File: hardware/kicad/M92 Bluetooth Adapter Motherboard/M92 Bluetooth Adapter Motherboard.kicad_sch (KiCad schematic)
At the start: 27 parts, among them IC1 PIC18F27Q43-I/SO, J2 Conn_Handset_RJ45, J6 Conn_MCU_Programming, J7 Conn_BT_Module, J8 Conn_MCU_IO_UART, Q2 PN2222ATA / MMBT2222A

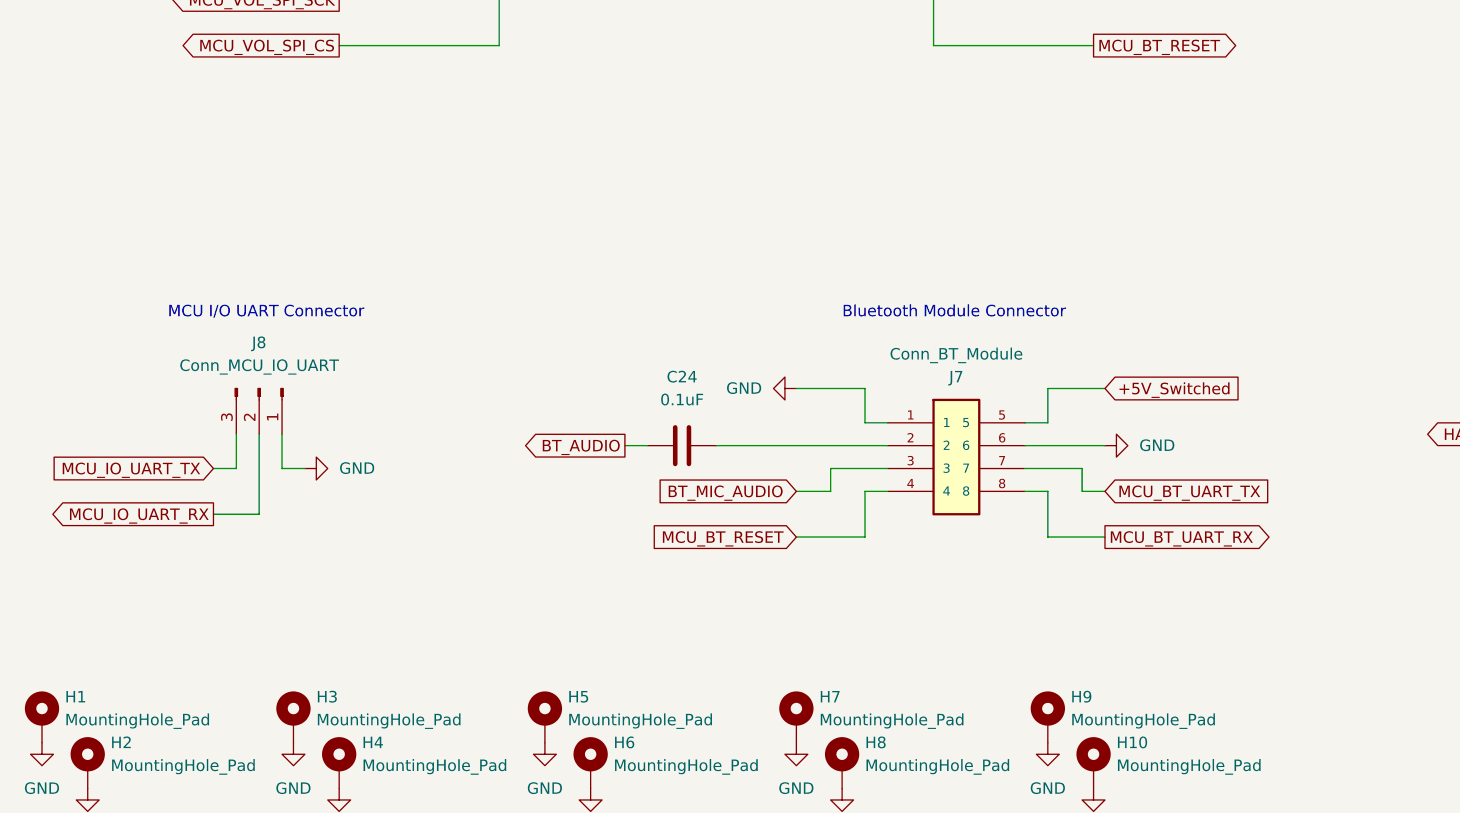
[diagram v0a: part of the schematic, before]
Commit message: Partial motherboard PCB updates for test fitting
This is a partial update to the motherboard PCB layout just so I can get some prototype boards manufactured and test fit with some updated/relocated components before committing to laying out the new custom battery/power management circuitry.

* Removed representation of Dayton Audio battery module PCB (will be replaced by custom battery circuitry in future).
* Relocated battery holders, and updated their footprints for sturdier part.
* Added pin headers for mounting the new programming port PCB.
* Adjusted positions of several mounting holes in attempt to match reality better (based on actual fitment of the PCB).
* Adjusted position of BT module connector slightly right in attempt to match reality better (based on actual fitment of the PCB).
* Adjusted footprint of mic jack to use oval PTH.
* Adjusted mic jack position further toward front edge of board to protrude more like original car phone mic jack.
* Added custom 3D models for BT module connector, RJ45 socket, and coax antenna port.
* Added coax antenna port and programming port to the PCB layout for spatial reference (not on schematic)
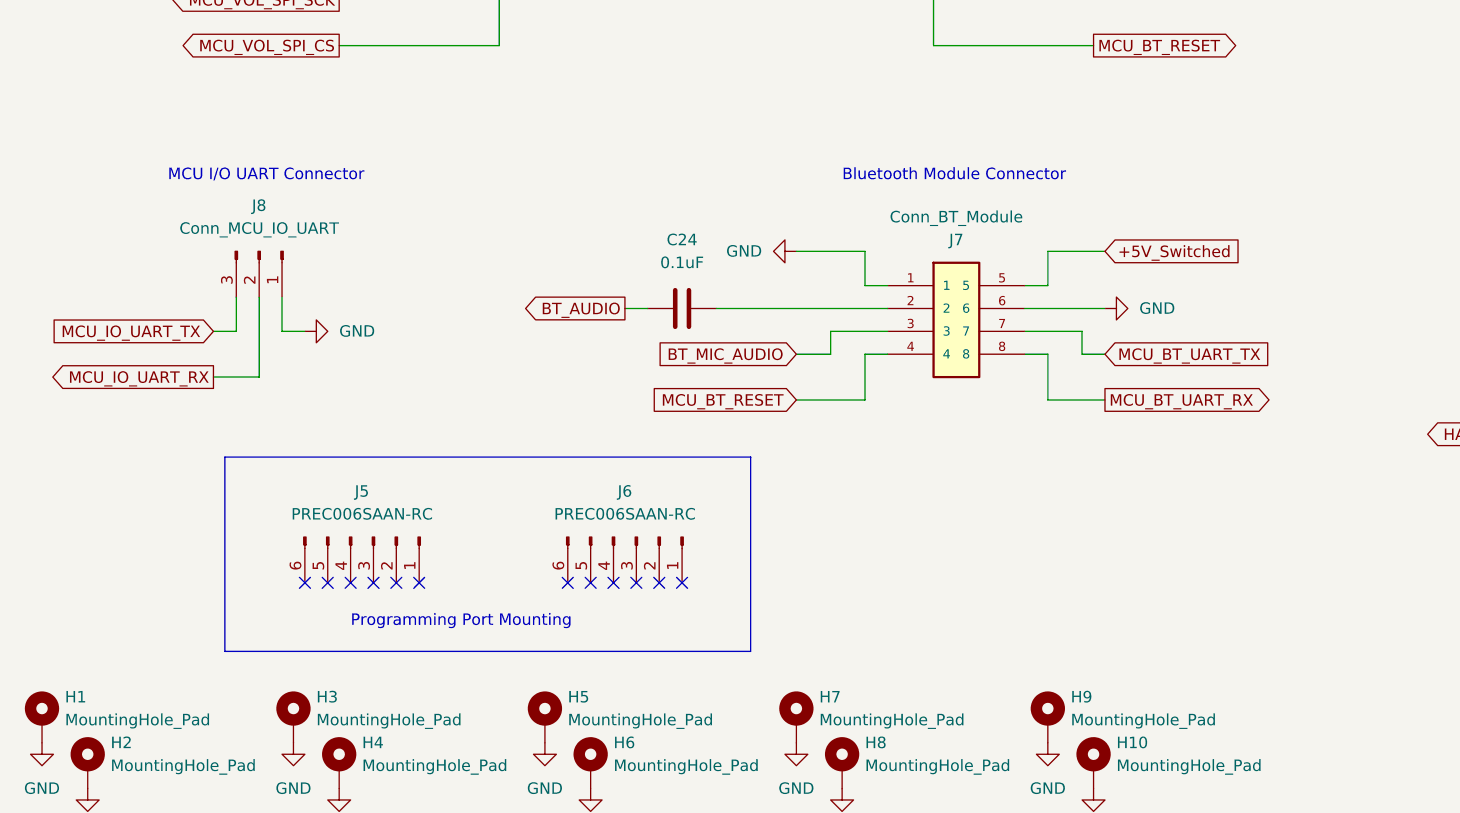
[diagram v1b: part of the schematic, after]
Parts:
- added J5, J6: PREC006SAAN-RC, Connector_PinHeader_2.54mm:PinHeader_1x06_P2.54mm_Vertical, symbol Connector:Conn_01x06_Pin
- H1, H10, H3, H4, H6, H7, H8, H9: footprint MountingHole:MountingHole_3.2mm_M3_Pad_Via -> MountingHole:MountingHole_3.2mm_M3_ISO14580_Pad
- J2: footprint GLXN88MBLK -> M92 Bluetooth Adapter Motherboard:KYCON_GLX-N-88M; symbol SamacSys_Parts:GLX-N-88M-BLK -> M92 Bluetooth Adapter Motherboard:GLX-N-88M; Manufacturer_Part_Number GLX-N-88M -> GLX-N-88M-BLK; Mouser Part Number 806-GLX-N-88M -> 806-GLX-N-88M-BLK; Mouser Price/Stock https://www.mouser.com/ProductDetail/Kycon/GLX-N-88M?qs=1jN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 -> https://www.mouser.com/ProductDetail/Kycon/GLX-N-88M-BLK?qs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
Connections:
- no-connect marks 2 -> 14
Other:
- note added: "Programming Port Mounting"
- moved on the sheet: C24, J7, J8

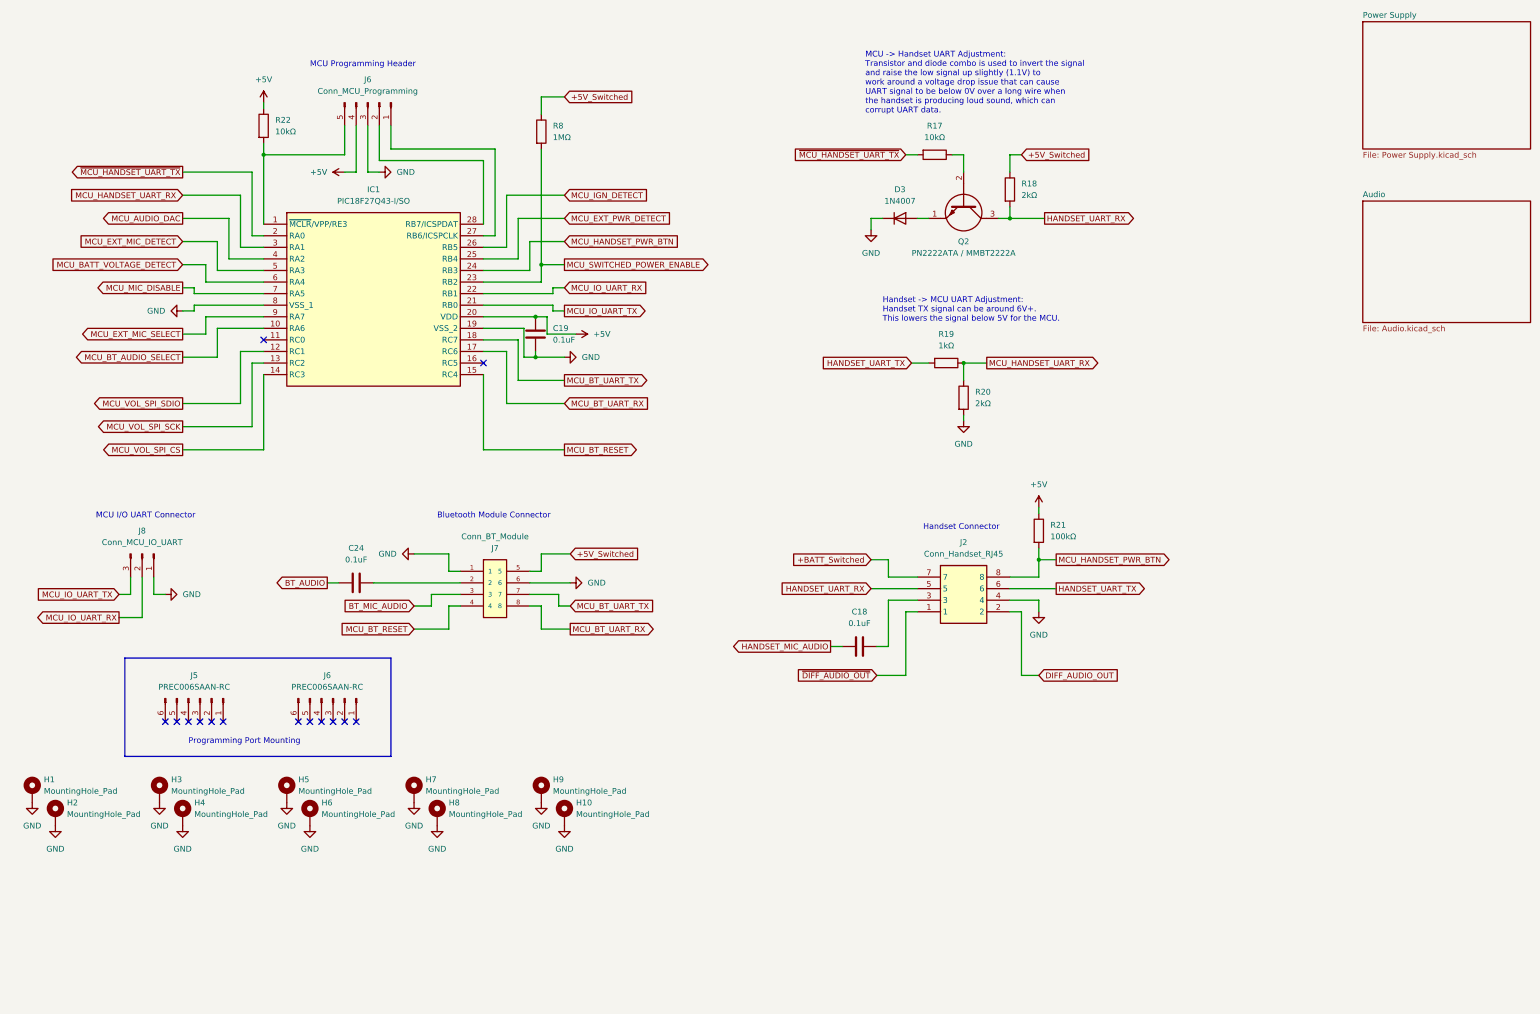
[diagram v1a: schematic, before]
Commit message: Add new battery module to motherboard schematic
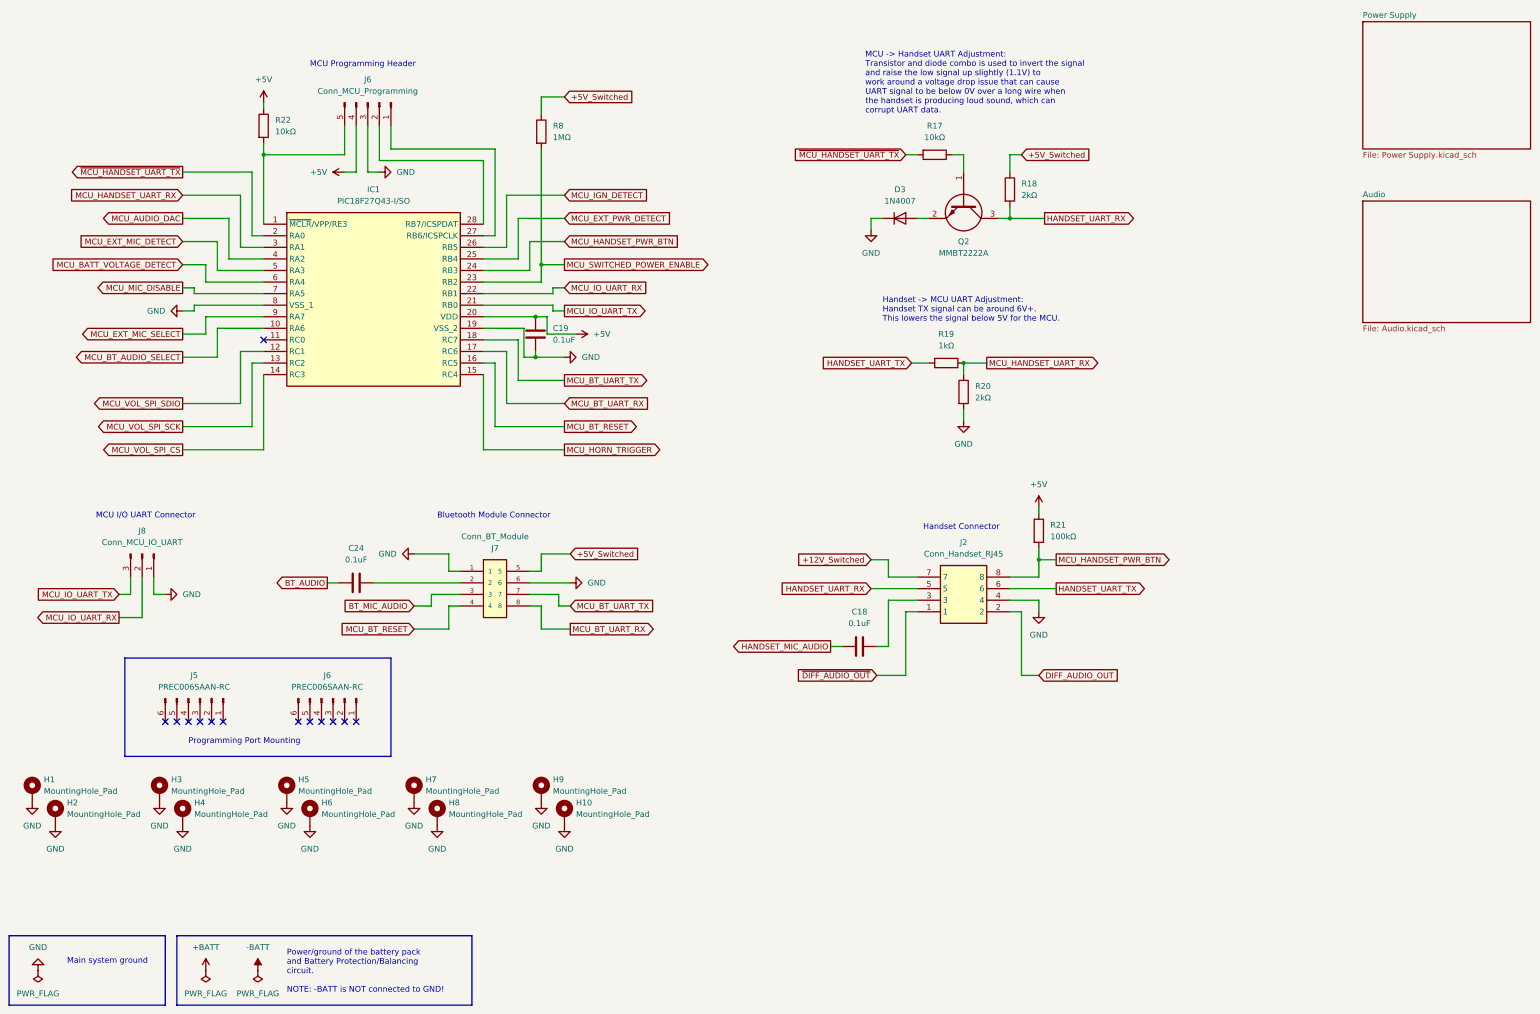
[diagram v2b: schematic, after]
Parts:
- Q2: value PN2222ATA / MMBT2222A -> MMBT2222A; footprint BC33740TA -> Package_TO_SOT_SMD:SOT-23-3; symbol SamacSys_Parts:PN2222ATA -> M92 Bluetooth Adapter Motherboard:BJT_N_BEC; JLCPCB Part # (none) -> C8512; Manufacturer (none) -> JCST; Manufacturer_Name onsemi -> (none); Manufacturer_Part_Number PN2222ATA -> MMBT2222A; Mouser Part Number 512-PN2222ATA -> (none); Mouser Price/Stock https://www.mouser.com/ProductDetail/onsemi-Fairchild/PN222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 -> (none)
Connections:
- net MCU_BT_RESET: now also IC1.16 (RC5); no longer IC1.15 (RC4)
- net at Q2.1 (B): now also R17.1; no longer D3.2 (A)
- net at Q2.2 (E): now also D3.2 (A); no longer R17.1
- net +BATT_Switched renamed +12V_Switched
- new net MCU_HORN_TRIGGER: IC1.15 (RC4)
- no-connect marks 14 -> 13
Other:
- note added: "Main system ground"
- note added: "Power/ground of the battery pack and Battery Protection/Balancing circuit. NOTE: -BATT is NOT connected to GND!"
- moved on the sheet: R20
